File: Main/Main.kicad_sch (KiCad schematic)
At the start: 0 parts

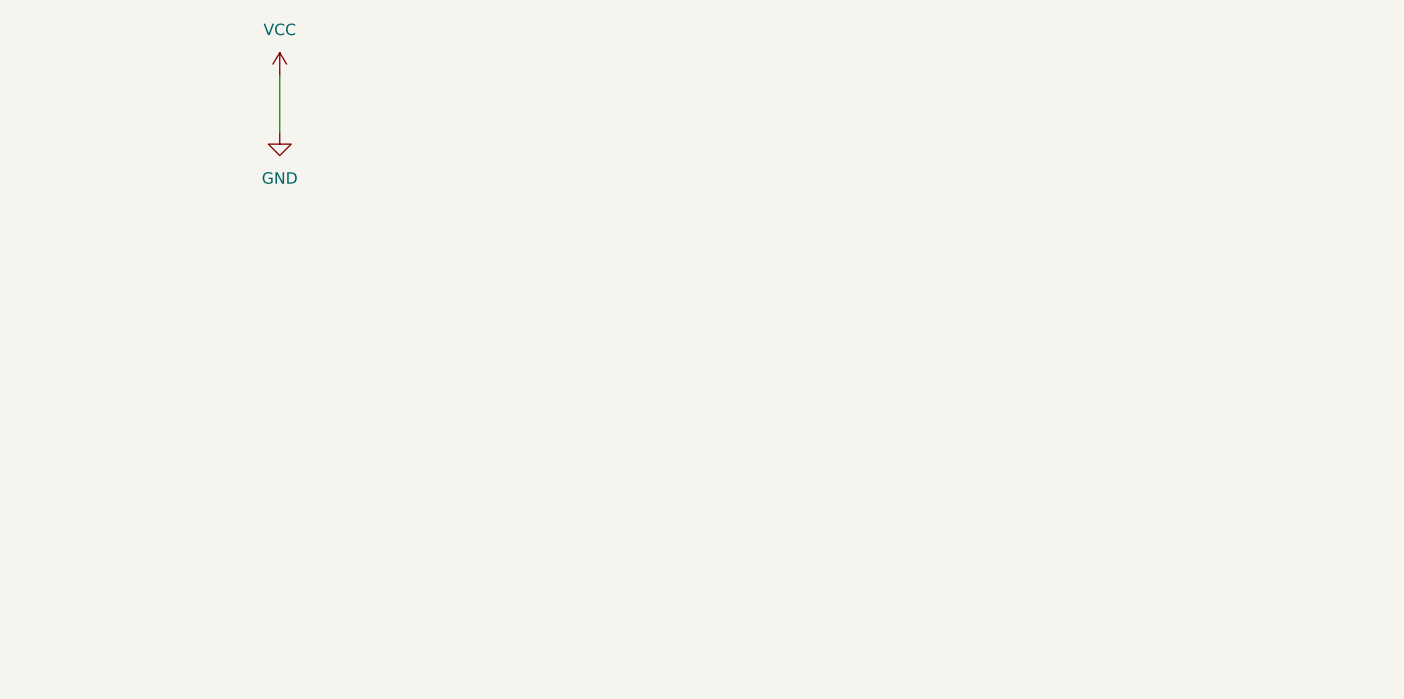
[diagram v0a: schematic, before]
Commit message: teensy symbol
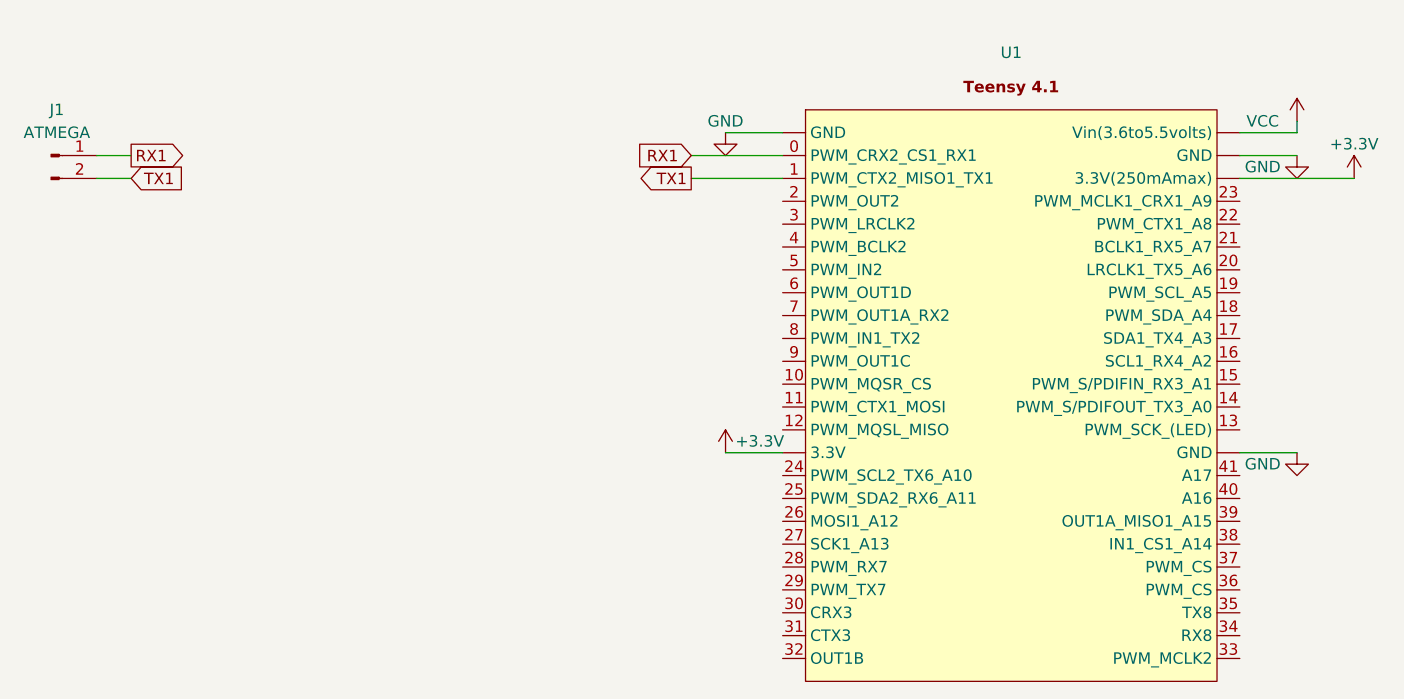
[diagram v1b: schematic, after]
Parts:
- added J1: ATMEGA, symbol Connector:Conn_01x02_Pin
- added U1: ~, symbol @admixSymbols:teensy_4.1
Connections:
- net GND: now also U1. (Vin(3.6to5.5volts))
- new net +3.3V: U1. (Vin(3.6to5.5volts))
- new net RX1: J1.1 (Pin_1), U1.0 (PWM_CRX2_CS1_RX1)
- new net TX1: J1.2 (Pin_2), U1.1 (PWM_CTX2_MISO1_TX1)
- new net VCC: U1. (Vin(3.6to5.5volts))

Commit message: tssp58038
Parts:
- added U10, U11, U12, U13, U14, U15, U2, U3, U4, U5, U6, U7, U8, U9: ~, symbol @admixSymbols:TSSP58038
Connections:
- net +3.3V: now also U10.3 (Vs), U11.3 (Vs), U12.3 (Vs), U13.3 (Vs), U14.3 (Vs), U15.3 (Vs), U2.3 (Vs), U3.3 (Vs), U4.3 (Vs), U5.3 (Vs), U6.3 (Vs), U7.3 (Vs), U8.3 (Vs), U9.3 (Vs)
- net GND: now also U10.2 (GND), U11.2 (GND), U12.2 (GND), U13.2 (GND), U14.2 (GND), U15.2 (GND), U2.2 (GND), U3.2 (GND), U4.2 (GND), U5.2 (GND), U6.2 (GND), U7.2 (GND), U8.2 (GND), U9.2 (GND)
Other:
- moved on the sheet: J1, U1

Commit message: ボルセンローパスフィルター
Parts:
- added C1, C10, C11, C12, C13, C14, C15, C16, C2, C3, C4, C5, C6, C7, C8, C9: 0.22uF, symbol Device:C
- added J2: 3.3Vin, symbol Connector:Conn_01x02_Pin
- added J3: Seeed Xiao, symbol Connector:Conn_01x02_Pin
- added R1, R10, R11, R12, R13, R14, R15, R16, R2, R3, R4, R5, R6, R7, R8, R9: 24k, symbol Device:R
- added U16, U17: ~, symbol @admixSymbols:TSSP58038
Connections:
- net +3.3V: now also J2.1 (Pin_1), U16.3 (Vs), U17.3 (Vs)
- net GND: now also C1.2, C10.2, C11.2, C12.2, C13.2, C14.2, C15.2, C16.2, C2.2, C3.2, C4.2, C5.2, C6.2, C7.2, C8.2, C9.2, J2.2 (Pin_2), U16.2 (GND), U17.2 (GND)
- net at U2.1 (OUT): now also R1.1
- net at U10.1 (OUT): now also R10.1
- net at U9.1 (OUT): now also R9.1
- net at U15.1 (OUT): now also R15.1
- net at U11.1 (OUT): now also R11.1
- net at U8.1 (OUT): now also R8.1
- net at U13.1 (OUT): now also R13.1
- net at U3.1 (OUT): now also R3.1
- net RX2: now reaches U1.7 (PWM_OUT1A_RX2)
- net RX2: now also J3.1 (Pin_1)
- net TX2: now reaches U1.8 (PWM_IN1_TX2)
- net TX2: now also J3.2 (Pin_2)
- net at U7.1 (OUT): now also R7.1
- net at U5.1 (OUT): now also R5.1
- net at U6.1 (OUT): now also R6.1
- net at U4.1 (OUT): now also R4.1
- net at U14.1 (OUT): now also R14.1
- net at U12.1 (OUT): now also R12.1
- new net: R2.1, U17.1 (OUT)
- new net: R16.1, U16.1 (OUT)
- new net BallSig1: C1.1, R1.2
- new net BallSig10: C10.1, R11.2
- new net BallSig11: C11.1, R12.2
- new net BallSig12: C12.1, R13.2
- new net BallSig13: C13.1, R14.2
- new net BallSig14: C14.1, R15.2
- new net BallSig15: C15.1, R16.2
- new net BallSig16: C16.1, R2.2
- new net BallSig2: C2.1, R3.2
- new net BallSig3: C3.1, R4.2
- new net BallSig4: C4.1, R5.2
- new net BallSig5: C5.1, R6.2
- new net BallSig6: C6.1, R7.2
- new net BallSig7: C7.1, R8.2
- new net BallSig8: C8.1, R9.2
- new net BallSig9: C9.1, R10.2
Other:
- note added: "Ballsensors"
- note added: "Connectors"
- note added: "MicroComputer"

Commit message: いろいろ
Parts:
- added C17: 10uF, symbol Device:C
- added D1: LED, symbol Device:LED
- added J4: AE-BNO055-BO, symbol Connector:Conn_01x04_Pin
- added J6: forCameraCPU, symbol Connector:Conn_01x02_Pin
- added SW1: SW_DPDT_x2, symbol Switch:SW_DPDT_x2
- C1, C10, C11, C12, C13, C14, C15, C16, C2, C3, C4, C5, C6, C7, C8, C9: value 0.22uF -> 0.33uF
- R1: value 24k -> 39k
- R10: renamed from R11; value 24k -> 39k
- R11: renamed from R12; value 24k -> 39k
- R12: renamed from R13; value 24k -> 39k
- R13: renamed from R14; value 24k -> 39k
- R14: renamed from R15; value 24k -> 39k
- R15: renamed from R16; value 24k -> 39k
- R16: renamed from R2; value 24k -> 39k
- R2: renamed from R3; value 24k -> 39k
- R3: renamed from R4; value 24k -> 39k
- R4: renamed from R5; value 24k -> 39k
- R5: renamed from R6; value 24k -> 39k
- R6: renamed from R7; value 24k -> 39k
- R7: renamed from R8; value 24k -> 39
- R8: renamed from R9; value 24k -> 39k
- R9: renamed from R10; value 24k -> 39k
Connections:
- net +3.3V: now also J4.1 (Pin_1)
- net BallSig1: now also U1.14 (PWM_S/PDIFOUT_TX3_A0)
- net BallSig10: now also U1.23 (PWM_MCLK1_CRX1_A9)
- net BallSig11: now also U1.26 (MOSI1_A12)
- net BallSig12: now also U1.27 (SCK1_A13)
- net BallSig13: now also U1.38 (IN1_CS1_A14)
- net BallSig14: now also U1.39 (OUT1A_MISO1_A15)
- net BallSig15: now also U1.40 (A16)
- net BallSig16: now also U1.41 (A17)
- net BallSig2: now also U1.15 (PWM_S/PDIFIN_RX3_A1)
- net BallSig3: now also U1.16 (SCL1_RX4_A2)
- net BallSig4: now also U1.17 (SDA1_TX4_A3)
- net BallSig5: now also U1.18 (PWM_SDA_A4)
- net BallSig6: now also U1.19 (PWM_SCL_A5)
- net BallSig7: now also U1.20 (LRCLK1_TX5_A6)
- net BallSig8: now also U1.21 (BCLK1_RX5_A7)
- net BallSig9: now also U1.22 (PWM_CTX1_A8)
- net GND: now also C17.2, J4.2 (Pin_2)
- net VCC: now also C17.1, SW1.1 (A), SW1.2 (B); no longer U1. (Vin(3.6to5.5volts))
- net SCL2: now reaches U1.24 (PWM_SCL2_TX6_A10)
- net SCL2: now also J4.4 (Pin_4)
- net SDA: now reaches U1.25 (PWM_SDA2_RX6_A11)
- net RX8: now reaches U1.34 (RX8)
- net RX8: now also J6.2 (Pin_2)
- net TX8: now reaches U1.35 (TX8)
- net TX8: now also J6.1 (Pin_1)
- new net: D1.1 (K), U1. (Vin(3.6to5.5volts))
- new net: D1.2 (A), SW1.3 (C)
- new net SDA2: J4.3 (Pin_3)
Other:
- moved on the sheet: U1

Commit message: 直接アップロード
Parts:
- removed C1, C10, C11, C12, C13, C14, C15, C16, C2, C3, C4, C5, C6, C7, C8, C9: 0.33uF, symbol Device:C
- removed D1: LED, symbol Device:LED
- removed J6: forCameraCPU, symbol Connector:Conn_01x02_Pin
- removed R10, R11, R12, R13, R14, R15, R16, R2, R3, R4, R5, R6, R8, R9: 39k, symbol Device:R
- removed R7: 39, symbol Device:R
- removed SW1: SW_DPDT_x2, symbol Switch:SW_DPDT_x2
- removed U10, U11, U12, U13, U14, U15, U16, U17, U2, U3, U4, U5, U6, U7, U8, U9: ~, symbol @admixSymbols:TSSP58038
- added D2: LED_Small, symbol Device:LED_Small
- added J5: ATMEGA_BALL, symbol Connector:Conn_01x02_Pin
- added SW1: SW_DIP_x01, symbol Switch:SW_DIP_x01
- J1: value ATMEGA -> ATMEGA_LINE
- J2: value 3.3Vin -> 3.3VinfromPS
- J3: value Seeed Xiao -> Seeed Xiao_UI
- R1: value 39k -> R
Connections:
- net +3.3V: now also R1.1; no longer J2.1 (Pin_1)
- net GND: now also SW1.2
- net VCC: now also J2.1 (Pin_1)
- net BallSig1: no longer names the net of R1.2
- net BallSig1: now also D2.2 (A), SW1.1; no longer U1.14 (PWM_S/PDIFOUT_TX3_A0)
- net BallSig10: no longer names the net of U1.23 (PWM_MCLK1_CRX1_A9)
- net BallSig11: no longer names the net of U1.26 (MOSI1_A12)
- net BallSig12: no longer names the net of U1.27 (SCK1_A13)
- net BallSig13: no longer names the net of U1.38 (IN1_CS1_A14)
- net BallSig14: no longer names the net of U1.39 (OUT1A_MISO1_A15)
- net BallSig15: no longer names the net of U1.40 (A16)
- net BallSig16: no longer names the net of U1.41 (A17)
- net BallSig2 renamed TX4ofMain
- net BallSig3: no longer names the net of U1.16 (SCL1_RX4_A2)
- net BallSig4: no longer names the net of U1.17 (SDA1_TX4_A3)
- net BallSig5: no longer names the net of U1.18 (PWM_SDA_A4)
- net BallSig6: no longer names the net of U1.19 (PWM_SCL_A5)
- net BallSig7: no longer names the net of U1.20 (LRCLK1_TX5_A6)
- net BallSig8: no longer names the net of U1.21 (BCLK1_RX5_A7)
- net BallSig9: no longer names the net of U1.22 (PWM_CTX1_A8)
- net RX1 renamed RX1ofMain
- net RX1ofMain: now also J5.1 (Pin_1)
- net RX2 renamed RX2ofMain
- net RX8: no longer names the net of U1.34 (RX8)
- net TX1 renamed TX1ofMain
- net TX1ofMain: now also J5.2 (Pin_2)
- net TX2 renamed TX2ofMain
- net TX8: no longer names the net of U1.35 (TX8)
- new net: D2.1 (K), U1. (Vin(3.6to5.5volts))
- new net RX4ofMain: U1.14 (PWM_S/PDIFOUT_TX3_A0)
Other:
- note added: "Main CPU"
- note removed: "Ballsensors"
- note removed: "MicroComputer"
- moved on the sheet: U1
